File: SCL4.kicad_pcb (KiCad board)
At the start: 2 copper layers, 150.5 x 233.3 mm, 38 parts, among them J1 spare1, J2 spare2, J3 Siemens_A1010-A263, J4 SP1, J5 SP2, J6 Conn_01x08, J7 5V out, U1 MC3487DX, U2 MC3487DX, U3 TRAM Size 2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

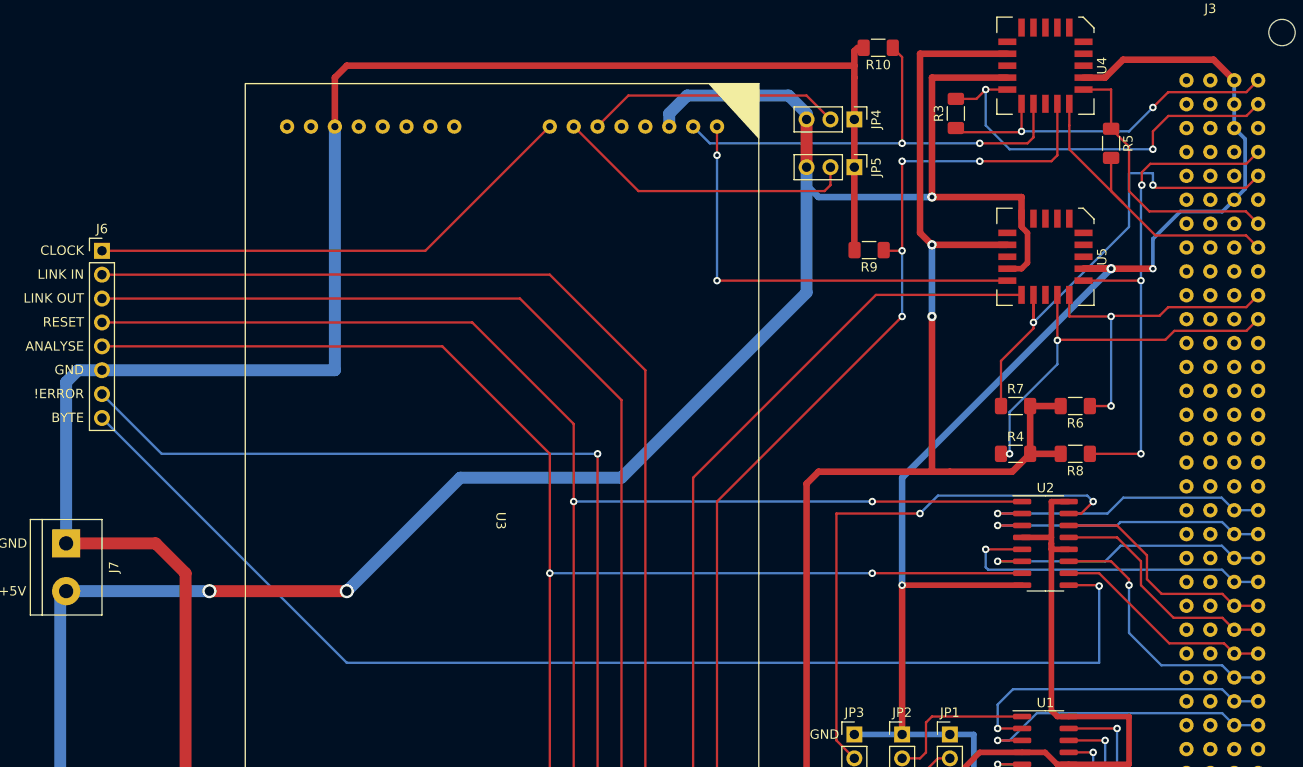
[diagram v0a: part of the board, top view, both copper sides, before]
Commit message: update 256pin connector
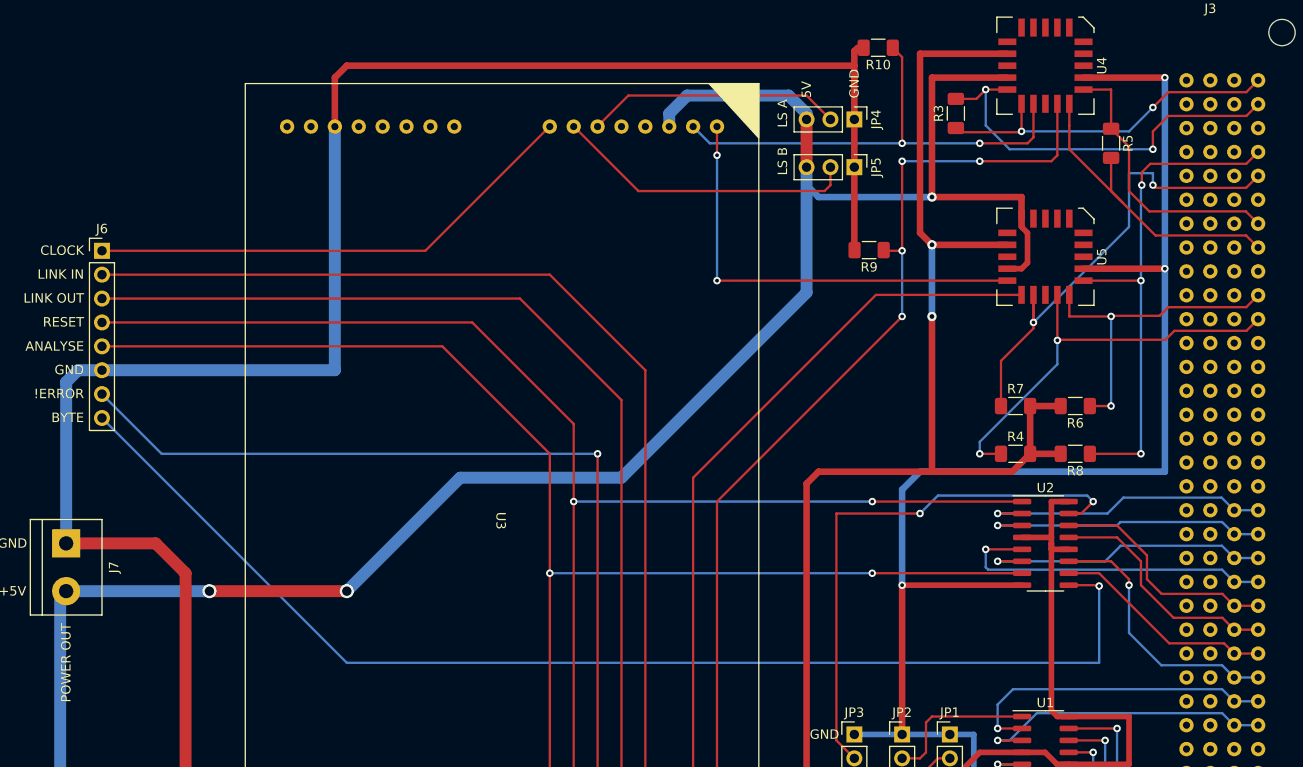
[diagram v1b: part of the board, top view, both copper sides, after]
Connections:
- J3 pad B1: GND -> unconnected-(J3-PadB1)
- J3 pad B2: GND -> unconnected-(J3-PadB2)
- J3 pad B3: GND -> unconnected-(J3-PadB3)
- J3 pad B6: GND -> unconnected-(J3-PadB6)
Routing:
- net //L3OUT: track 42.2 -> 44.9 mm
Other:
- board text added: "5V"
- board text added: "LS A"
- board text added: "LS B"
- board text added: "POWER OUT"
